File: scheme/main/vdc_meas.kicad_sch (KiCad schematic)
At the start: 24 parts, among them U12 AMC1311, U13 RS8551

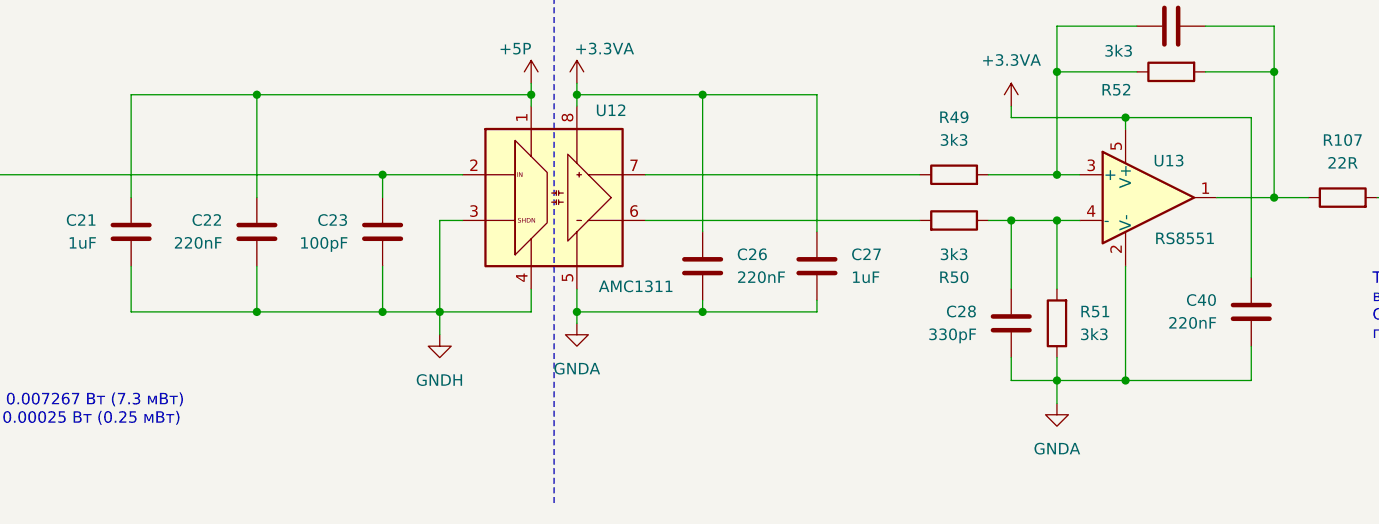
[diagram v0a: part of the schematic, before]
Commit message: replace some 220n capacitors with 100n
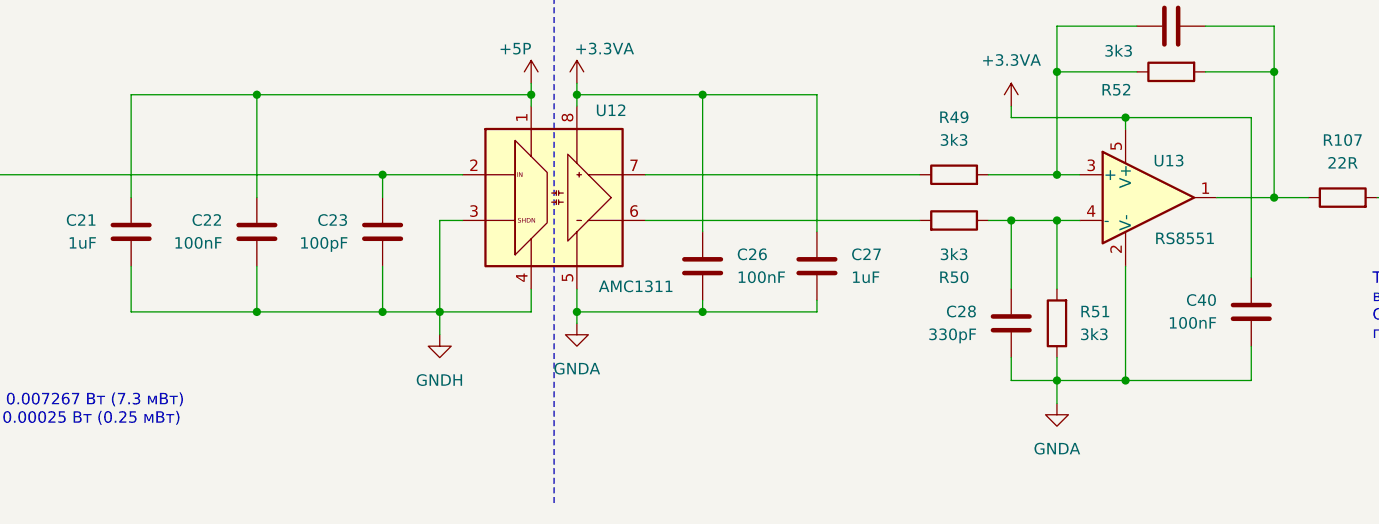
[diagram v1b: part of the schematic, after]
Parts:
- C22, C26, C40: value 220nF -> 100nF
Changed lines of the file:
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@@
 			)
 		)
-		(property "Value" "220nF"
+		(property "Value" "100nF"
 			(at 156.21 88.8999 0)
 			(effects
@@
 			)
 		)
-		(property "Value" "220nF"
+		(property "Value" "100nF"
 			(at 99.06 85.0899 0)
 			(effects
@@
 			)
 		)
-		(property "Value" "220nF"
+		(property "Value" "100nF"
 			(at 209.55 93.9799 0)
 			(effects

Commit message: sheets titles
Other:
- title: (none) -> Измерение напряжения звена постоянного тока
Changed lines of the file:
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@@
 	(generator_version "8.0")
 	(paper "A4")
+	(title_block
+		(title "Измерение напряжения звена постоянного тока")
+	)
 	(junction
 		(at 67.31 77.47)
